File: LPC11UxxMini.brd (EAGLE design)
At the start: 20.3 x 40.6 mm, 39 parts, among them Q1 BC857B, U1 LPC11Uxx, U2 MCP1252-33X50I/MS, Y1 12MHz

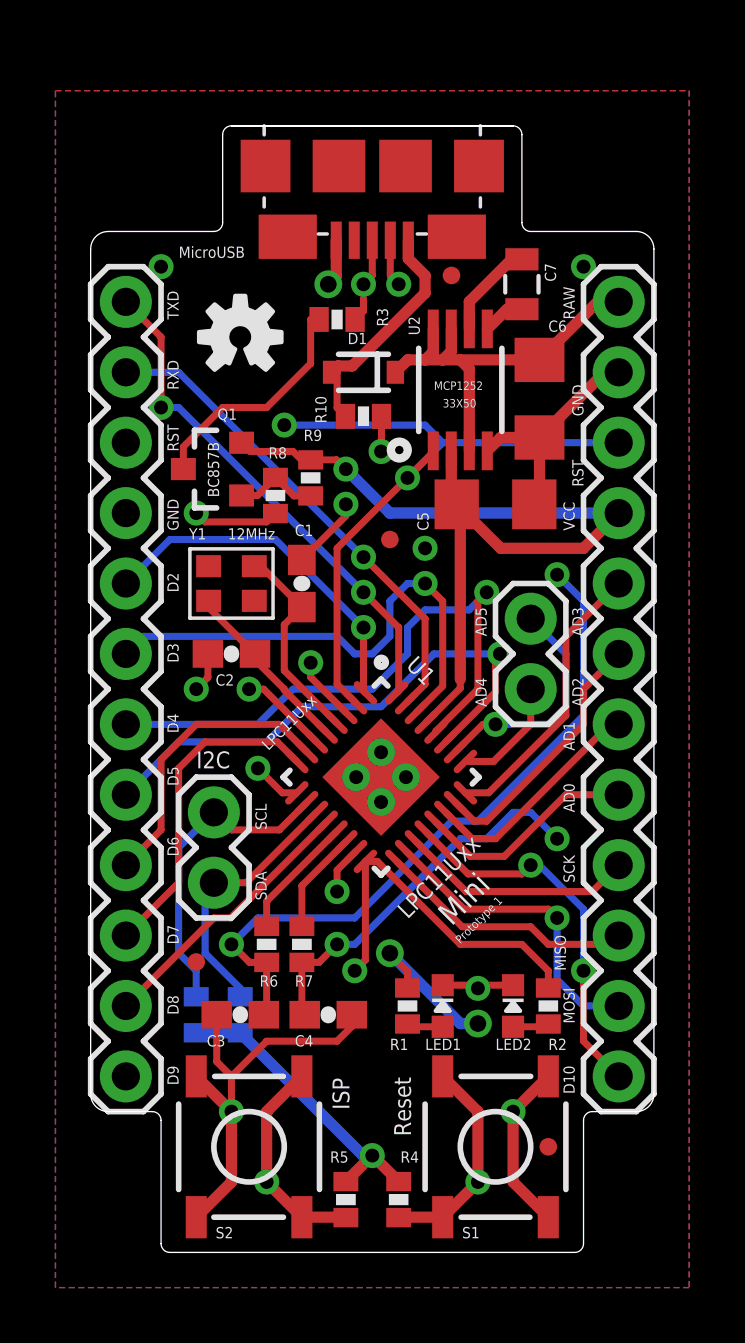
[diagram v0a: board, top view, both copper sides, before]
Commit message: Squished to true Arduino Pro Mini form factor (Prototype 2)
also added pin_map.txt
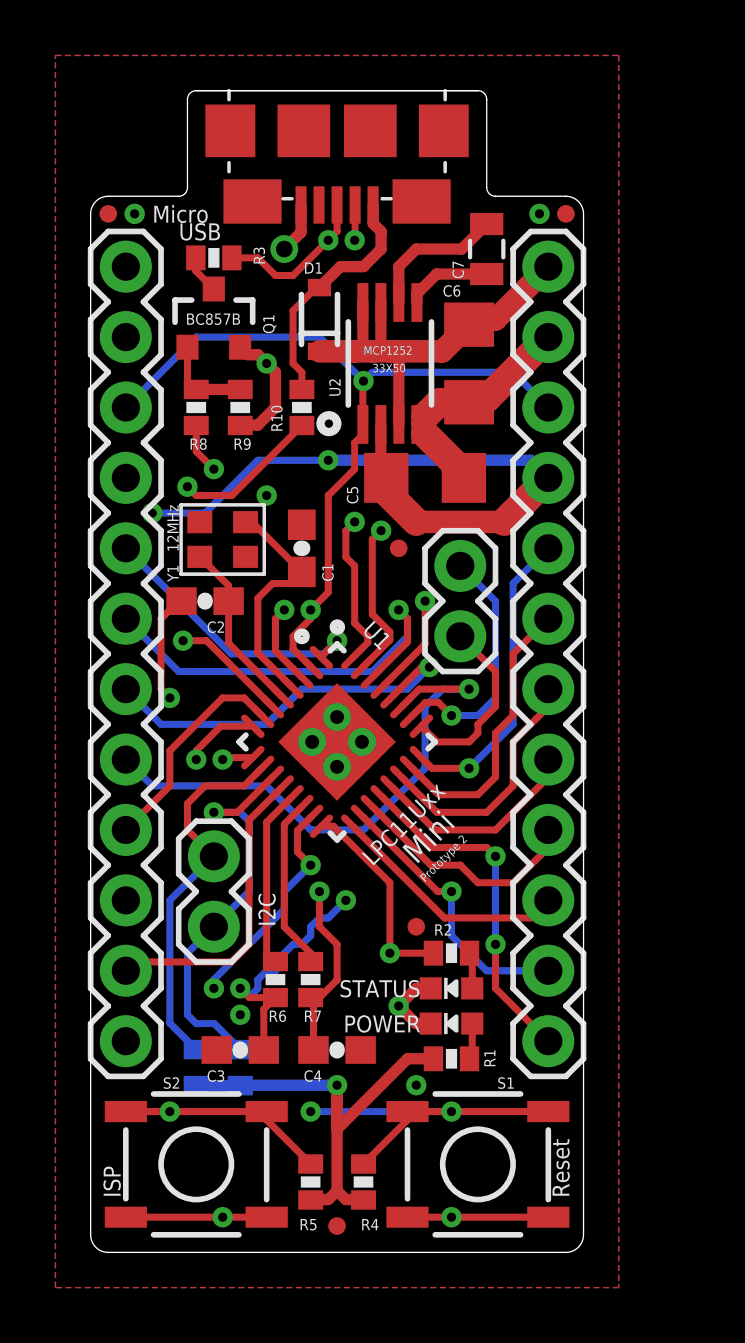
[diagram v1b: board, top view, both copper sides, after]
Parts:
- removed LED1, LED2: 20mA, microbuilder:CHIPLED_0603_NOOUTLINE
- removed U$5: (no value), SparkFun-Aesthetics:OSHW-LOGO-S
- added JP9: FIDUCIALUFIDUCIAL, SparkFun-Aesthetics:MICRO-FIDUCIAL
- added POWER, STATUS: 20mA, microbuilder:CHIPLED_0603_NOOUTLINE
- moved JP3 30.1 mm to (17.1, 37.5)
- moved JP7 14.0 mm to (11.7, 11.7)
- moved JP8 12.6 mm to (0.64, 37.5)
- moved JP6 8.14 mm to (8.89, 0.95)
- moved Q1 5.40 mm to (4.45, 33.7), turned to 0 degrees
- moved R3 4.97 mm to (4.45, 35.9)
- moved R8 4.27 mm to (3.81, 30.5)
- moved R2 3.98 mm to (13.0, 10.8), turned to 0 degrees
- moved R9 3.59 mm to (5.40, 30.5), turned to 270 degrees
- moved JP5 3.18 mm to (13.3, 22.2)
- moved C6 2.84 mm to (13.7, 32.1)
- moved JP2 2.84 mm to (16.5, 7.62)
- moved U2 2.71 mm to (10.8, 32.1)
- moved C5 2.71 mm to (12.1, 27.9)
- moved R1 2.48 mm to (13.0, 6.99), turned to 0 degrees
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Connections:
- removed net LED1_RESISTOR: LED1.A, R1.2
- removed net LED2_RESISTOR: LED2.A, R2.2
- new net POWER_LED_RESISTOR: POWER.A, R1.2
- new net STATUS_LED_RESISTOR: R2.2, STATUS.A
- net GND: now also POWER.C, STATUS.C; no longer LED1.C, LED2.C
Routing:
- net GND: track 39.6 -> 27.7 mm, vias 9 -> 10
- net USB_CONNECT: track 21.6 -> 30.2 mm, vias 2 -> 3
- net D4: track 21.3 -> 14.1 mm
- net RST: track 68.3 -> 61.0 mm, vias 3 -> 4
- net USB_CONNECT_COLLECTOR: track 8.53 -> 1.39 mm
- net SDA: track 9.52 -> 14.4 mm, vias 0 -> 1
- net ISP: track 36.9 -> 32.1 mm
- net D7: track 11.8 -> 8.85 mm, vias 0 -> 1
- net D9: track 22.8 -> 25.6 mm
- net D3: track 18.4 -> 15.6 mm
- net D2: track 12.9 -> 10.2 mm
- net AD4: track 4.18 -> 6.78 mm
- net D6: track 10.5 -> 7.93 mm
- net MC_USB_DP: track 3.71 -> 6.27 mm
- net MC_USB_VBUS: track 19.9 -> 17.3 mm
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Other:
- board size 20.3 x 40.6 mm -> 17.8 x 41.9 mm
- board text added: "/LPC11UxxMini"
- board text added: "I2C"
- board text added: "Logxen"
- board text added: "Micro"
- board text added: "Prototype 2"
- board text added: "Reprap community"
- board text added: "USB"
- board text added: "designed by"
- board text added: "http://github.com/logxen"
- board text added: "with the help of the"
- board text removed: "Designed by Logxen"
- board text removed: "MicroUSB"
- board text removed: "Prototype 1"
- board text removed: "http://github.com/logxen/lpc11uxx_breakout"
- board text removed: "with the help of the Reprap community"

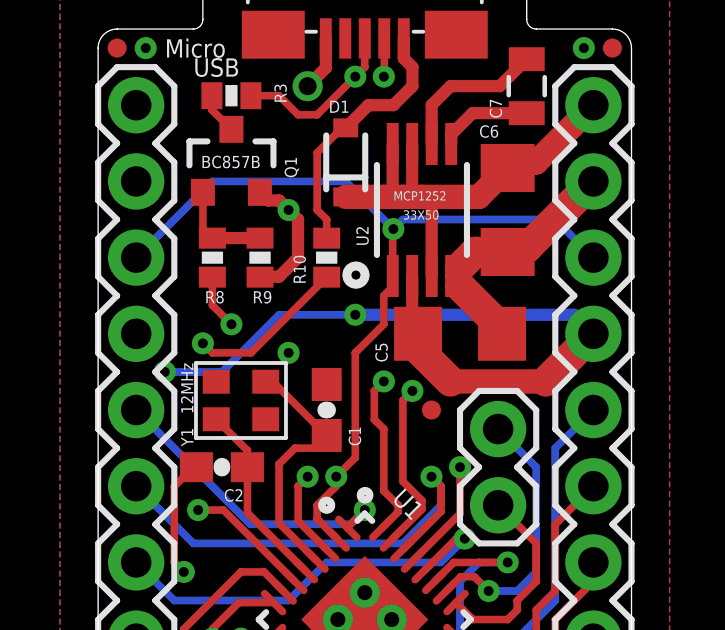
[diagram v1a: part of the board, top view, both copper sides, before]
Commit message: Added pull-down to P0_3 USB_VBUS
leaving P0_3 floating does not seem to reliably select serial
programming mode vs. usb programming mode, so a 10k pull-down was added
to assert serial mode when usb power is not present.
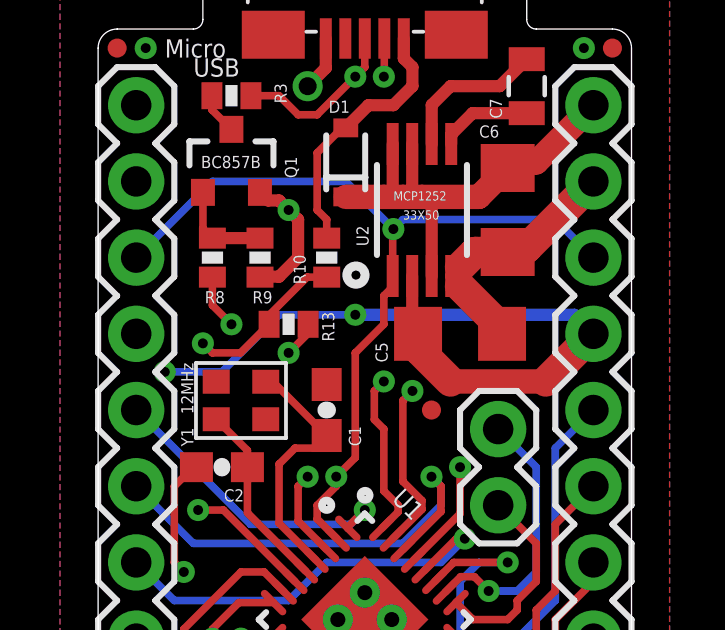
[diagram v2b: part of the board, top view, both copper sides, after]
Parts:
- added R13: 10kOhm, SparkFun-Resistors:0402-RES
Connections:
- net GND: now also R13.1
- net MC_USB_VBUS: now also R13.2
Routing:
- net GND: track 27.7 -> 29.0 mm
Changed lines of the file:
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@@
 <?xml version="1.0" encoding="utf-8"?>
 <!DOCTYPE eagle SYSTEM "eagle.dtd">
-<eagle version="6.4">
+<eagle version="6.3">
 <drawing>
 <settings>
@@
 </element>
 <element name="JP9" library="SparkFun-Aesthetics" package="MICRO-FIDUCIAL" value="FIDUCIALUFIDUCIAL" x="11.1125" y="25.4"/>
+<element name="R13" library="SparkFun-Resistors" package="0402-RES" value="10kOhm" x="6.35" y="28.2575" smashed="yes" rot="R180">
+<attribute name="NAME" x="7.874" y="27.686" size="0.4064" layer="25" rot="R90"/>
+<attribute name="VALUE" x="7.4295" y="29.4005" size="0.4064" layer="27" rot="R180"/>
+</element>
 </elements>
 <signals>
@@
 <via x="11.7475" y="6.0325" extent="1-16" drill="0.3302"/>
 <via x="16.1925" y="37.465" extent="1-16" drill="0.3302"/>
+<contactref element="R13" pad="1"/>
+<wire x1="7" y1="28.2575" x2="7" y2="27.955" width="0.254" layer="1"/>
+<wire x1="7" y1="27.955" x2="6.35" y2="27.305" width="0.254" layer="1"/>
 </signal>
 <signal name="XTALOUT">
@@
 <wire x1="5.08" y1="18.0975" x2="5.08" y2="21.59" width="0.254" layer="3"/>
 <wire x1="5.08" y1="21.59" x2="3.175" y2="23.495" width="0.254" layer="3"/>
-<wire x1="7.62" y1="29.83" x2="5.095" y2="27.305" width="0.254" layer="1"/>
-<wire x1="5.095" y1="27.305" x2="3.81" y2="27.305" width="0.254" layer="1"/>
 <wire x1="3.81" y1="27.305" x2="3.4925" y2="27.6225" width="0.254" layer="1"/>
 <via x="3.4925" y="27.6225" extent="1-16" drill="0.3302"/>
@@
 <wire x1="5.849440625" y1="17.8493125" x2="4.8318125" y2="17.8493125" width="0.254" layer="1"/>
 <wire x1="4.8318125" y1="17.8493125" x2="4.7625" y2="17.78" width="0.254" layer="1"/>
+<contactref element="R13" pad="2"/>
+<wire x1="3.81" y1="27.305" x2="4.7475" y2="27.305" width="0.254" layer="1"/>
+<wire x1="4.7475" y1="27.305" x2="5.7" y2="28.2575" width="0.254" layer="1"/>
+<wire x1="7.62" y1="29.83" x2="6.97" y2="29.83" width="0.254" layer="1"/>
+<wire x1="6.97" y1="29.83" x2="5.7" y2="28.56" width="0.254" layer="1"/>
+<wire x1="5.7" y1="28.2575" x2="5.7" y2="28.56" width="0.254" layer="1"/>
 </signal>
 <signal name="USB_VBUS">
